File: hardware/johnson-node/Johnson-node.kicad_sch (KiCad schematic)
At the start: 0 parts

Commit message: hats
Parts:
- added C1, C13, C19, C20: 1u, Capacitor_SMD:C_0603_1608Metric, symbol Device:C
- added C10: 4.7u, Capacitor_SMD:C_0603_1608Metric, symbol Device:C
- added C11, C12, C21, C22, C3, C7, C8: 0.1u, Capacitor_SMD:C_0603_1608Metric, symbol Device:C
- added C15: 2.2u, Capacitor_SMD:C_0603_1608Metric, symbol Device:C
- added C16, C17, C4, C9: 100n, Capacitor_SMD:C_0603_1608Metric, symbol Device:C
- added C18, C2, C5: 10u, Capacitor_SMD:C_0603_1608Metric, symbol Device:C
- added C6: 22u, Capacitor_SMD:C_0603_1608Metric, symbol Device:C
- added IC1, IC2: ADC124S051CIMM_NOPB, CustomFootprints:SOP50P490X110-10N, symbol ADC124S051CIMM_NOPB:ADC124S051CIMM_NOPB
- added J1: Conn_01x02, Connector_JST:JST_XA_S02B-XASK-1_1x02_P2.50mm_Horizontal, symbol Connector_Generic:Conn_01x02
- added J10, J11, J2, J3, J4, J5, J6, J7, J8, J9: Conn_01x03, Connector_JST:JST_XA_S03B-XASK-1_1x03_P2.50mm_Horizontal, symbol Connector_Generic:Conn_01x03
- added J12: Conn_01x12, Connector_JST:JST_XA_B12B-XASK-1_1x12_P2.50mm_Vertical, symbol Connector_Generic:Conn_01x12
- added J13: BSEL, Connector_PinHeader_2.54mm:PinHeader_1x02_P2.54mm_Vertical, symbol Connector_Generic:Conn_01x02
- added J14: RST, Connector_PinHeader_2.54mm:PinHeader_1x02_P2.54mm_Vertical, symbol Connector_Generic:Conn_01x02
- added L1: 2.2u, Inductor_SMD:L_0603_1608Metric, symbol Device:L
- added L2: 5.6u, Inductor_SMD:L_0603_1608Metric, symbol Device:L
- added R1, R2: 27, Resistor_SMD:R_0603_1608Metric, symbol Device:R
- added R3: 10k, Resistor_SMD:R_0603_1608Metric, symbol Device:R
- added R7: 0, Resistor_SMD:R_0603_1608Metric, symbol Device:R
- added U1: ESP32-S3-WROOM-1U-N4R2, CustomFootprints:XCVR_ESP32-S3-WROOM-1U-N4R2, symbol ESP32-S3-WROOM-1U-N4R2:ESP32-S3-WROOM-1U-N4R2
- added U2: LMR50410Y3FQDBVRQ1, CustomFootprints:SOT95P280X145-6N, symbol LMR50410Y3FQDBVRQ1:LMR50410Y3FQDBVRQ1
- added U3: LMR50410Y5FQDBVRQ1, Custom_MSM:Regulator_Switching_SOT-23-6, symbol LMR50410Y3FQDBVRQ1:LMR50410Y3FQDBVRQ1
- added U4: ISO1042BQDWVQ1, CustomFootprints:DWV0008A-MFG, symbol 2025-11-15_02-18-59:ISO1042BQDWVQ1
- added U5: MAX3390EEUD_T, CustomFootprints:SOP65P640X110-14N, symbol MAX3390EEUD_T:MAX3390EEUD_T
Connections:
- new net: C17.1, L1.1, U2.6 (SW)
- new net: C17.2, U2.1 (CB)
- new net: IC1.10 (SCLK), IC2.10 (SCLK)
- new net: IC1.9 (DOUT), IC2.9 (DOUT)
- new net: C4.1, L2.1, U3.6 (SW)
- new net: C4.2, U3.1 (CB)
- new net: R2.1, U1.14 (IO20)
- new net: R7.2, U3.4 (EN)
- new net: J13.2 (Pin_2), U1.27 (IO0)
- new net: R1.1, U1.13 (IO19)
- new net +3V3: C11.1, C18.1, C2.2, C3.2, C8.2, L1.2, R3.1, U1.2 (3V3), U2.3 (FB), U4.1 (VCC1), U5.1 (VL), U5.8 (~{THREE}-STATE)
- new net +5V: C10.2, C12.1, C13.1, C6.1, C7.2, J10.3 (Pin_3), J11.3 (Pin_3), J2.3 (Pin_3), J3.3 (Pin_3), J4.3 (Pin_3), J5.3 (Pin_3), J6.3 (Pin_3), J7.3 (Pin_3), J8.3 (Pin_3), J9.3 (Pin_3), L2.2, U3.3 (FB), U4.8 (VCC2), U5.14 (VCC)
- new net +5V_Supply: C19.1, C20.1, C21.1, C22.1, IC1.2 (VA), IC2.2 (VA)
- new net BATT: C15.1, C16.1, C5.1, C9.1, J1.2 (Pin_2), R7.1, U2.4 (EN), U2.5 (VIN), U3.5 (VIN)
- new net CAND: U1.39 (IO1), U4.2 (TXD)
- new net CANH: U4.7 (CANH)
- new net CANL: U4.6 (CANL)
- new net CANR: U1.38 (IO2), U4.3 (RXD)
- new net CS: U1.18 (IO10), U5.5 (I_VL4)
- new net CS1: IC1.1 (~{CS})
- new net CS2: IC2.1 (~{CS})
- new net DIN: IC1.8 (DIN), IC2.8 (DIN)
- new net DOWN: U1.25 (IO48)
- new net DOWN_LED: U1.6 (IO6)
- new net E_CS: U5.10 (O_VCC4)
- new net E_MISO: U5.13 (I_VCC1)
- new net E_MOSI: U5.12 (O_VCC2)
- new net E_SCLK: U5.11 (O_VCC3)
- new net FLATSHIFT: U1.12 (IO8)
- new net GND: C1.1, C10.1, C11.2, C12.2, C13.2, C15.2, C16.2, C18.2, C19.2, C2.1, C20.2, C21.2, C22.2, C3.1, C5.2, C6.2, C7.1, C8.1, C9.2, IC1.3 (GND), IC2.3 (GND), J1.1 (Pin_1), J10.1 (Pin_1), J11.1 (Pin_1), J13.1 (Pin_1), J14.1 (Pin_1), J2.1 (Pin_1), J3.1 (Pin_1), J4.1 (Pin_1), J5.1 (Pin_1), J6.1 (Pin_1), J7.1 (Pin_1), J8.1 (Pin_1), J9.1 (Pin_1), U1.1 (GND), U1.40 (GND__1), U1.41_1 (GND__2), U1.41_2 (GND__3), U1.41_3 (GND__4), U1.41_4 (GND__5), U1.41_5 (GND__6), U1.41_6 (GND__7), U1.41_7 (GND__8), U1.41_8 (GND__9), U1.41_9 (GND__10), U2.2 (GND), U3.2 (GND), U4.4 (GND1), U4.5 (GND2), U5.7 (GND)
- new net MISO: U1.21 (IO13), U5.2 (O_VL1)
- new net MOSI: U1.19 (IO11), U5.3 (I_VL2)
- new net Main_Reset: C1.2, J14.2 (Pin_2), R3.2, U1.3 (EN)
- new net NEUTRAL: U1.26 (IO45)
- new net NEUTRAL_LED: U1.5 (IO5)
- new net PWM: U1.17 (IO9)
- new net RX: U1.36 (RXD0)
- new net SCLK: U1.20 (IO12), U5.4 (I_VL3)
- new net SGAOUT: IC1.7 (IN1)
- new net SGBOUT: IC1.6 (IN2)
- new net SGCOUT: IC1.5 (IN3)
- new net SGDOUT: IC1.4 (IN4)
- new net SGEOUT: IC2.7 (IN1)
- new net SGFOUT: IC2.6 (IN2)
- new net SGGOUT: IC2.5 (IN3)
- new net SGHOUT: IC2.4 (IN4)
- new net TX: U1.37 (TXD0)
- new net UP: U1.24 (IO47)
- new net UP_LED: U1.7 (IO7)
- new net USBD+: R2.2
- new net USBD-: R1.2
- no-connect marks 0 -> 17

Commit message: finish schem
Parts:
- removed J12: Conn_01x12, Connector_JST:JST_XA_B12B-XASK-1_1x12_P2.50mm_Vertical, symbol Connector_Generic:Conn_01x12
- added C14, C23: 0.1u, Capacitor_SMD:C_0603_1608Metric, symbol Device:C
- added C24: 1u, Capacitor_SMD:C_0603_1608Metric, symbol Device:C
- added C25, C26, C27, C28, C29, C30, C31, C32: 33n, symbol Device:C
- added D1, D2, D3, D4, D5, D6, D7, D8: D_Schottky, symbol Device:D_Schottky
- added D10, D11, D9: RED LED, LED_SMD:LED_0603_1608Metric, symbol Device:LED
- added J15: SO4B-XASK-1, Connector_JST:JST_XA_S04B-XASK-1_1x04_P2.50mm_Horizontal, symbol Connector_Generic:Conn_01x04
- added J16: Conn_01x02, Connector_JST:JST_XA_S02B-XASK-1_1x02_P2.50mm_Horizontal, symbol Connector_Generic:Conn_01x02
- added J17: Conn_01x14, Connector_JST:JST_XA_S14B-XASK-1_1x14_P2.50mm_Horizontal, symbol Connector_Generic:Conn_01x14
- added R10, R11, R12, R4, R5, R6, R8, R9: 100R, symbol Device:R
- added R13: 120, symbol Device:R
- added R14, R15: 5k1, Resistor_SMD:R_0603_1608Metric, symbol Device:R
- added R16, R18: 270R, Resistor_SMD:R_0603_1608Metric, symbol Device:R
- added R17: 620R, Resistor_SMD:R_0603_1608Metric, symbol Device:R
- added U6: MAX3390EEUD_T, CustomFootprints:SOP65P640X110-14N, symbol MAX3390EEUD_T:MAX3390EEUD_T
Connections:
- net E_CS is gone; now on net 5V_CS_A: U5.10 (O_VCC4)
- net E_MISO is gone; now on net 5V_MISO: U5.13 (I_VCC1)
- net E_MOSI is gone; now on net 5V_MOSI: U5.12 (O_VCC2)
- net E_SCLK is gone; now on net 5V_SCLK: U5.11 (O_VCC3)
- net +3V3: now also C14.1, R16.1, U6.1 (VL), U6.8 (~{THREE}-STATE)
- net +5V: now also C23.1, C24.1, D1.1 (K), D2.1 (K), D3.1 (K), D4.1 (K), D5.1 (K), D6.1 (K), D7.1 (K), D8.1 (K), J16.2 (Pin_2), R17.1, U6.14 (VCC); no longer J10.3 (Pin_3), J11.3 (Pin_3)
- net CANH: now also J10.3 (Pin_3), J11.3 (Pin_3), R13.1
- net CANL: now also J10.2 (Pin_2), J11.2 (Pin_2), R13.2
- net GND: now also C14.2, C23.2, C24.2, C25.2, C26.2, C27.2, C28.2, C29.2, C30.2, C31.2, C32.2, D10.1 (K), D11.1 (K), D9.1 (K), J16.1 (Pin_1), J17.12 (Pin_12), J17.14 (Pin_14), R14.2, R15.1, U6.7 (GND)
- net USBD+: now also J15.1 (Pin_1)
- net USBD-: now also J15.2 (Pin_2)
- net SGC: now reaches J3.2 (Pin_2)
- net SGC: now also R9.1
- net 5V_SCLK: now reaches IC1.10 (SCLK), IC2.10 (SCLK)
- net 5V_SCLK: now also J17.3 (Pin_3)
- net 5V_MISO: now reaches IC1.9 (DOUT), IC2.9 (DOUT)
- net 5V_MISO: now also J17.4 (Pin_4)
- net SGD: now reaches J5.2 (Pin_2)
- net SGD: now also R11.1
- net SGB: now reaches J4.2 (Pin_2)
- net SGB: now also R5.1
- net SGG: now reaches J8.2 (Pin_2)
- net SGG: now also R10.1
- net SGE: now reaches J6.2 (Pin_2)
- net SGE: now also R6.1
- net SGF: now reaches J7.2 (Pin_2)
- net SGF: now also R8.1
- net at U1.28 (IO35): now also R18.1
- net SGA: now reaches J2.2 (Pin_2)
- net SGA: now also R4.1
- net SGH: now reaches J9.2 (Pin_2)
- net SGH: now also R12.1
- net CS renamed CS_A
- net CS1 renamed 5V_CS_A
- net CS2 renamed 5V_CS_B
- net 5V_CS_B: now also U6.12 (O_VCC2)
- net DIN renamed 5V_MOSI
- net 5V_MOSI: now also J17.5 (Pin_5)
- net DOWN: no longer names the net of U1.25 (IO48)
- net DOWN_LED: no longer names the net of U1.6 (IO6)
- net FLATSHIFT renamed CS_C
- net CS_C: now also U6.4 (I_VL3)
- net NEUTRAL: no longer names the net of U1.26 (IO45)
- net NEUTRAL_LED: no longer names the net of U1.5 (IO5)
- net PWM renamed CS_B
- net CS_B: now also U6.3 (I_VL2)
- net SGAOUT renamed SGA_P
- net SGA_P: now also C25.1, D1.2 (A), R4.2
- net SGBOUT renamed SGB_P
- net SGB_P: now also C26.1, D2.2 (A), R5.2
- net SGCOUT renamed SGC_P
- net SGC_P: now also C29.1, D5.2 (A), R9.2
- net SGDOUT renamed SGD_P
- net SGD_P: now also C31.1, D7.2 (A), R11.2
- net SGEOUT renamed SGE_P
- net SGE_P: now also C27.1, D3.2 (A), R6.2
- net SGFOUT renamed SGF_P
- net SGF_P: now also C28.1, D4.2 (A), R8.2
- net SGGOUT renamed SGG_P
- net SGG_P: now also C30.1, D6.2 (A), R10.2
- net SGHOUT renamed SGH_P
- net SGH_P: now also C32.1, D8.2 (A), R12.2
- net UP: no longer names the net of U1.24 (IO47)
- net UP_LED renamed CS_D
- net CS_D: now also U6.5 (I_VL4)
- new net: D9.2 (A), R16.2
- new net: J15.4 (Pin_4), R14.1
- new net: D11.2 (A), R18.2
- new net: J15.3 (Pin_3), R15.2
- new net: D10.2 (A), R17.2
- new net +12V: J17.11 (Pin_11), J17.13 (Pin_13)
- new net 5V_CS_C: J17.1 (Pin_1), U6.11 (O_VCC3)
- new net 5V_CS_D: J17.2 (Pin_2), U6.10 (O_VCC4)
- no-connect marks 17 -> 23
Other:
- moved on the sheet: C1, C11, C12, C13, C2, C3, J10, J11, J13, J14, R1, R2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

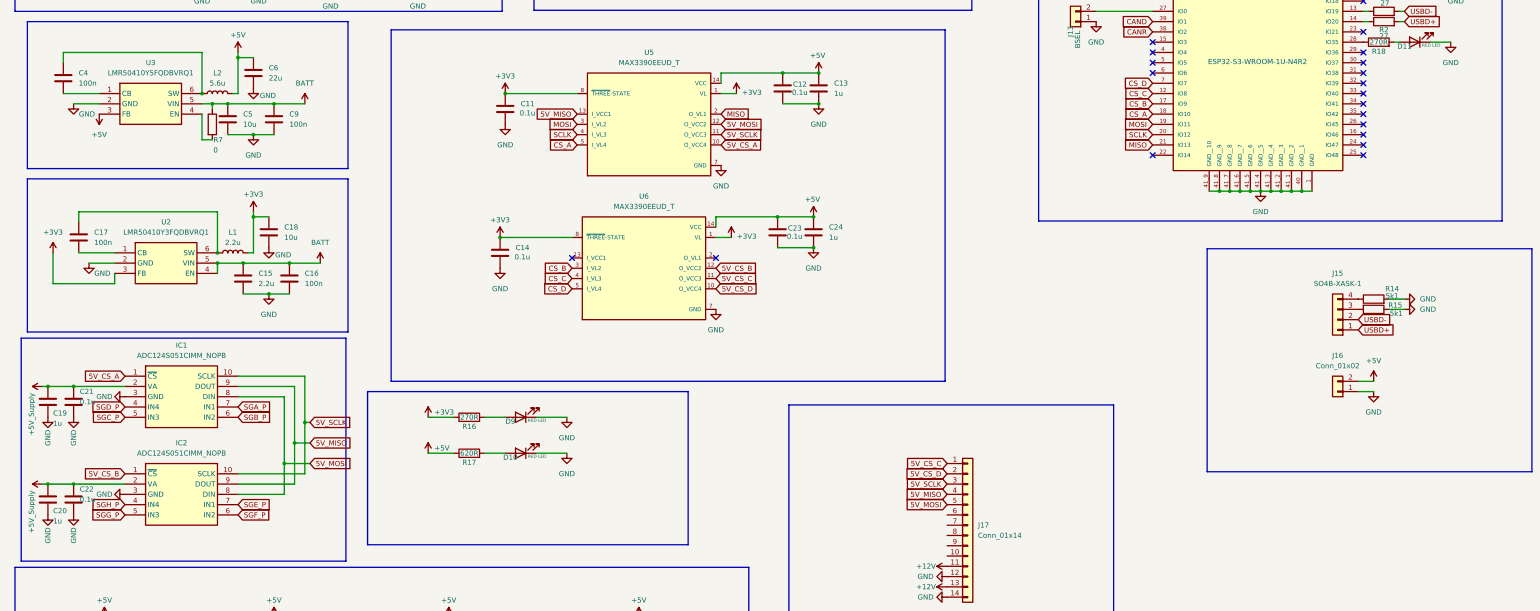
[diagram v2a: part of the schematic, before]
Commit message: placement of components
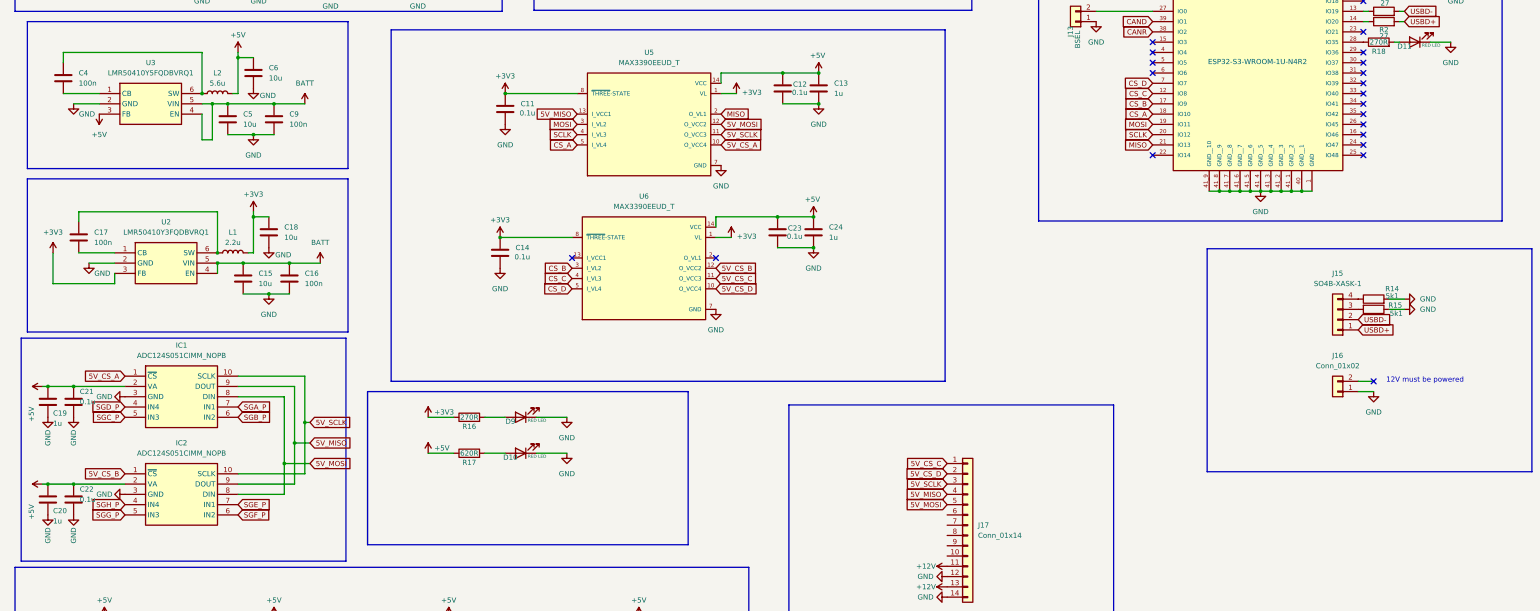
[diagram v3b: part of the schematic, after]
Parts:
- removed R7: 0, Resistor_SMD:R_0603_1608Metric, symbol Device:R
- C15: value 2.2u -> 10u
- C25, C26, C27, C28, C29, C30, C31, C32: footprint (none) -> Capacitor_SMD:C_0603_1608Metric
- C6: value 22u -> 10u
- D1, D2, D3, D4, D5, D6, D7, D8: footprint (none) -> Diode_SMD:D_0603_1608Metric
- J17: footprint Connector_JST:JST_XA_S14B-XASK-1_1x14_P2.50mm_Horizontal -> Connector_JST:JST_XA_B14B-XASK-1_1x14_P2.50mm_Vertical
- L1, L2: footprint Inductor_SMD:L_0603_1608Metric -> CustomFootprints:Shielded_Inductor_SMD_7265
- R10, R11, R12, R13, R4, R5, R6, R8, R9: footprint (none) -> Resistor_SMD:R_0603_1608Metric
- U3: footprint Custom_MSM:Regulator_Switching_SOT-23-6 -> CustomFootprints:SOT95P280X145-6N
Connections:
- net +5V_Supply is gone; now on net +5V: C19.1, C20.1, C21.1, C22.1, IC1.2 (VA), IC2.2 (VA)
- net +5V: no longer J16.2 (Pin_2)
- net BATT: now also U3.4 (EN)
- no-connect marks 23 -> 24
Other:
- note added: "12V must be powered"
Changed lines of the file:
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@@
 		)
 	)
+	(text "12V must be powered"
+		(exclude_from_sim no)
+		(at 363.22 149.606 0)
+		(effects
+			(font
+				(size 1.27 1.27)
+			)
+		)
+	)
 	(junction
 		(at 60.96 78.74)
@@
 		(at 347.98 83.82)
 	)
+	(no_connect
+		(at 350.52 149.86)
+	)
 	(wire
 		(pts
@@
 	(wire
 		(pts
-			(xy 63.5 81.28) (xy 63.5 82.55)
+			(xy 63.5 81.28) (xy 63.5 90.17)
 		)
 		(stroke
@@
 			)
 		)
-		(property "Value" "2.2u"
+		(property "Value" "10u"
 			(at 74.93 125.7299 0)
 			(show_name no)
@@
 			)
 		)
-		(property "Footprint" ""
+		(property "Footprint" "Resistor_SMD:R_0603_1608Metric"
 			(at 161.29 251.968 90)
 			(hide yes)
@@
 			)
 		)
-		(property "Footprint" "Connector_JST:JST_XA_S14B-XASK-1_1x14_P2.50mm_Horizontal"
+		(property "Footprint" "Connector_JST:JST_XA_B14B-XASK-1_1x14_P2.50mm_Vertical"
 			(at 250.19 185.42 0)
 			(hide yes)
@@
 			)
 		)
-		(property "Footprint" "Inductor_SMD:L_0603_1608Metric"
+		(property "Footprint" "CustomFootprints:Shielded_Inductor_SMD_7265"
 			(at 64.77 78.74 0)
 			(hide yes)
@@
 			)
 		)
-		(property "Footprint" ""
+		(property "Footprint" "Diode_SMD:D_0603_1608Metric"
 			(at 36.83 243.84 0)
 			(hide yes)
@@
 			)
 		)
-		(property "Footprint" ""
+		(property "Footprint" "Resistor_SMD:R_0603_1608Metric"
 			(at 160.02 217.678 90)
 			(hide yes)
@@
 	)
 	(symbol
-		(lib_id "Device:R")
-		(at 63.5 86.36 0)
-		(unit 1)
-		(body_style 1)
-		(exclude_from_sim no)
-		(in_bom yes)
-		(on_board yes)
-		(in_pos_files yes)
-		(dnp no)
-		(property "Reference" "R7"
-			(at 63.754 90.17 0)
-			(show_name no)
-			(do_not_autoplace no)
-			(effects
-				(font
-					(size 1.27 1.27)
-				)
-				(justify left)
-			)
-		)
-		(property "Value" "0"
-			(at 63.754 92.71 0)
-			(show_name no)
-			(do_not_autoplace no)
-			(effects
-				(font
-					(size 1.27 1.27)
-				)
-				(justify left)
-			)
-		)
-		(property "Footprint" "Resistor_SMD:R_0603_1608Metric"
-			(at 61.722 86.36 90)
-			(hide yes)
-			(show_name no)
-			(do_not_autoplace no)
-			(effects
-				(font
-					(size 1.27 1.27)
-				)
-			)
-		)
-		(property "Datasheet" ""
-			(at 63.5 86.36 0)
-			(hide yes)
-			(show_name no)
-			(do_not_autoplace no)
-			(effects
-				(font
-					(size 1.27 1.27)
-				)
-			)
-		)
-		(property "Description" "Resistor"
-			(at 63.5 86.36 0)
-			(hide yes)
-			(show_name no)
-			(do_not_autoplace no)
-			(effects
-				(font
-					(size 1.27 1.27)
-				)
-			)
-		)
-		(pin "1"
-		)
-		(pin "2"
-		)
-		(instances
-			(project "Johnson-node"
-				(path "/68fcba3f-8847-4595-9e16-ef770a2b1abc"
-					(reference "R7")
-					(unit 1)
-				)
-			)
-		)
-	)
-	(symbol
 		(lib_id "Device:C")
 		(at 116.84 254 0)
@@
 			)
 		)
-		(property "Footprint" ""
+		(property "Footprint" "Capacitor_SMD:C_0603_1608Metric"
 			(at 117.8052 257.81 0)
 			(hide yes)
@@
 			)
 		)
-		(property "Footprint" ""
+		(property "Footprint" "Diode_SMD:D_0603_1608Metric"
 			(at 36.83 212.09 0)
 			(hide yes)
@@
 			)
 		)
-		(property "Value" "22u"
+		(property "Value" "10u"
 			(at 77.47 74.9299 0)
 			(show_name no)
@@
 			)
 		)
-		(property "Value" "+5V_Supply"
+		(property "Value" "+5V"
 			(at 18.796 157.988 0)
 			(show_name no)
@@
 			)
 		)
-		(property "Footprint" ""
+		(property "Footprint" "Resistor_SMD:R_0603_1608Metric"
 			(at 27.94 217.678 90)
 			(hide yes)
@@
 			)
 		)
-		(property "Value" "+5V_Supply"
+		(property "Value" "+5V"
 			(at 18.796 182.118 0)
 			(show_name no)
@@
 			)
 		)
-		(property "Footprint" ""
+		(property "Footprint" "Capacitor_SMD:C_0603_1608Metric"
 			(at 166.0652 257.81 0)
 			(hide yes)
@@
 			)
 		)
-		(property "Footprint" ""
+		(property "Footprint" "Resistor_SMD:R_0603_1608Metric"
 			(at 225.552 48.26 90)
 			(hide yes)
@@
 			)
 		)
-		(property "Footprint" ""
+		(property "Footprint" "Diode_SMD:D_0603_1608Metric"
 			(at 121.92 246.38 0)
 			(hide yes)
@@
 			)
 		)
-		(property "Footprint" ""
+		(property "Footprint" "Resistor_SMD:R_0603_1608Metric"
 			(at 113.03 217.678 90)
 			(hide yes)
@@
 			)
 		)
-		(property "Footprint" ""
+		(property "Footprint" "Capacitor_SMD:C_0603_1608Metric"
 			(at 32.7152 223.52 0)
 			(hide yes)
@@
 			)
 		)
-		(property "Footprint" ""
+		(property "Footprint" "Diode_SMD:D_0603_1608Metric"
 			(at 78.74 212.09 0)
 			(hide yes)
@@
 			)
 		)
-		(property "Footprint" ""
+		(property "Footprint" "Capacitor_SMD:C_0603_1608Metric"
 			(at 164.7952 223.52 0)
 			(hide yes)
@@
 			)
 		)
-		(property "Footprint" ""
+		(property "Footprint" "Diode_SMD:D_0603_1608Metric"
 			(at 121.92 212.09 0)
 			(hide yes)
@@
 			)
 		)
-		(property "Footprint" ""
+		(property "Footprint" "Resistor_SMD:R_0603_1608Metric"
 			(at 27.94 249.428 90)
 			(hide yes)
@@
 			)
 		)
-		(property "Footprint" ""
+		(property "Footprint" "Diode_SMD:D_0603_1608Metric"
 			(at 170.18 246.38 0)
 			(hide yes)
@@
 			)
 		)
-		(property "Footprint" ""
+		(property "Footprint" "Diode_SMD:D_0603_1608Metric"
 			(at 168.91 212.09 0)
 			(hide yes)
@@
 			)
 		)
-		(property "Footprint" "Custom_MSM:Regulator_Switching_SOT-23-6"
+		(property "Footprint" "CustomFootprints:SOT95P280X145-6N"
 			(at 57.15 173.66 0)
 			(hide yes)
@@
 			)
 		)
-		(property "Footprint" ""
+		(property "Footprint" "Capacitor_SMD:C_0603_1608Metric"
 			(at 72.0852 256.54 0)
 			(hide yes)
@@
 			)
 		)
-		(property "Footprint" ""
+		(property "Footprint" "Resistor_SMD:R_0603_1608Metric"
 			(at 69.85 217.678 90)
 			(hide yes)
@@
 			)
 		)
-		(property "Footprint" ""
+		(property "Footprint" "Capacitor_SMD:C_0603_1608Metric"
 			(at 32.7152 255.27 0)
 			(hide yes)
@@
 	)
 	(symbol
-		(lib_id "power:+5V")
-		(at 350.52 149.86 0)
-		(unit 1)
-		(body_style 1)
-		(exclude_from_sim no)
-		(in_bom yes)
-		(on_board yes)
-		(in_pos_files yes)
-		(dnp no)
-		(fields_autoplaced yes)
-		(property "Reference" "#PWR031"
-			(at 350.52 153.67 0)
-			(hide yes)
-			(show_name no)
-			(do_not_autoplace no)
-			(effects
-				(font
-					(size 1.27 1.27)
-				)
-			)
-		)
-		(property "Value" "+5V"
-			(at 350.52 144.78 0)
-			(show_name no)
-			(do_not_autoplace no)
-			(effects
-				(font
-					(size 1.27 1.27)
-				)
-			)
-		)
-		(property "Footprint" ""
-			(at 350.52 149.86 0)
-			(hide yes)
-			(show_name no)
-			(do_not_autoplace no)
-			(effects
-				(font
-					(size 1.27 1.27)
-				)
-			)
-		)
-		(property "Datasheet" ""
-			(at 350.52 149.86 0)
-			(hide yes)
-			(show_name no)
-			(do_not_autoplace no)
-			(effects
-				(font
-					(size 1.27 1.27)
-				)
-			)
-		)
-		(property "Description" "Power symbol creates a global label with name \"+5V\""
-			(at 350.52 149.86 0)
-			(hide yes)
-			(show_name no)
-			(do_not_autoplace no)
-			(effects
-				(font
-					(size 1.27 1.27)
-				)
-			)
-		)
-		(pin "1"
-		)
-		(instances
-			(project "Johnson-node"
-				(path "/68fcba3f-8847-4595-9e16-ef770a2b1abc"
-					(reference "#PWR031")
-					(unit 1)
-				)
-			)
-		)
-	)
-	(symbol
 		(lib_id "power:+3V3")
 		(at 347.98 43.18 0)
@@
 			)
 		)
-		(property "Footprint" ""
+		(property "Footprint" "Resistor_SMD:R_0603_1608Metric"
 			(at 67.31 250.698 90)
 			(hide yes)
@@
 			)
 		)
-		(property "Footprint" ""
+		(property "Footprint" "Capacitor_SMD:C_0603_1608Metric"
 			(at 74.6252 223.52 0)
 			(hide yes)
@@
 			)
 		)
-		(property "Footprint" ""
+		(property "Footprint" "Resistor_SMD:R_0603_1608Metric"
 			(at 113.03 251.968 90)
 			(hide yes)
@@
 			)
 		)
-		(property "Footprint" ""
+		(property "Footprint" "Diode_SMD:D_0603_1608Metric"
 			(at 76.2 245.11 0)
 			(hide yes)
@@
 			)
 		)
-		(property "Footprint" "Inductor_SMD:L_0603_1608Metric"
+		(property "Footprint" "CustomFootprints:Shielded_Inductor_SMD_7265"
 			(at 68.58 118.11 0)
 			(hide yes)
@@
 			)
 		)
-		(property "Footprint" ""
+		(property "Footprint" "Capacitor_SMD:C_0603_1608Metric"
 			(at 117.8052 223.52 0)
 			(hide yes)
